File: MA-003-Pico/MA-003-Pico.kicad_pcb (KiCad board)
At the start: 2 copper layers, 49.5 x 80 mm, 5 parts, among them M1 rs485_ttl_module, M2 rs485_ttl_module, M3 rs485_ttl_module, M4 rs485_ttl_module

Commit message: Some more work
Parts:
- removed M1, M2, M3, M4: rs485_ttl_module, RS485ToTTL:rs485_ttl_module
- added H1: MountingHole_Pad, MountingHole:MountingHole_2.7mm_M2.5_DIN965_Pad, F.Cu at (138.4, 61.6)
- added H2: MountingHole_Pad, MountingHole:MountingHole_2.7mm_M2.5_DIN965_Pad, F.Cu at (175.9, 61.6)
- added H3: MountingHole_Pad, MountingHole:MountingHole_2.7mm_M2.5_DIN965_Pad, F.Cu at (177.2, 123.2)
- added H4: MountingHole_Pad, MountingHole:MountingHole_2.7mm_M2.5_DIN965_Pad, F.Cu at (139.1, 123.8)
- added J1: Power, Connector_Molex:Molex_KK-254_AE-6410-03A_1x03_P2.54mm_Vertical, F.Cu at (139.7, 68.6)
- added J2: I2C, Connector_Molex:Molex_KK-254_AE-6410-04A_1x04_P2.54mm_Vertical, F.Cu at (174.6, 76.2)
- added J3: Interface_A, Connector_IDC:IDC-Header_2x05_P2.54mm_Vertical, F.Cu at (138.4, 88.3)
- added J4: Interface_B, Connector_IDC:IDC-Header_2x05_P2.54mm_Vertical, F.Cu at (176.5, 99.1)
- added J5: Power_IB, Connector_PinHeader_2.54mm:PinHeader_1x03_P2.54mm_Vertical, F.Cu at (178.4, 107.3)
- added J6: Power_IA, Connector_PinHeader_2.54mm:PinHeader_1x03_P2.54mm_Vertical, F.Cu at (136.5, 80.0)
- added J7: Pico_On/Off, Connector_PinHeader_2.54mm:PinHeader_1x02_P2.54mm_Vertical, F.Cu at (174.6, 112.4)
- added J8: WS2812, Connector_Molex:Molex_KK-254_AE-6410-03A_1x03_P2.54mm_Vertical, F.Cu at (137.8, 109.9)
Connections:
- A1 pad 1: unconnected-(A1-GPIO0-Pad1) -> /GPIO_1
- A1 pad 10: unconnected-(A1-GPIO7-Pad10) -> /GPIO_8
- A1 pad 11: unconnected-(A1-GPIO8-Pad11) -> /GPIO_9
- A1 pad 12: unconnected-(A1-GPIO9-Pad12) -> /GPIO_10
- A1 pad 13: Net-(A1-GND-Pad13) -> /GND
- A1 pad 14: unconnected-(A1-GPIO10-Pad14) -> /GPIO_11
- A1 pad 15: unconnected-(A1-GPIO11-Pad15) -> /GPIO_12
- A1 pad 16: unconnected-(A1-GPIO12-Pad16) -> /GPIO_13
- A1 pad 17: unconnected-(A1-GPIO13-Pad17) -> /GPIO_14
- A1 pad 18: Net-(A1-GND-Pad13) -> /GND
- A1 pad 19: unconnected-(A1-GPIO14-Pad19) -> /GPIO_15
- A1 pad 2: unconnected-(A1-GPIO1-Pad2) -> /GPIO_2
- A1 pad 20: unconnected-(A1-GPIO15-Pad20) -> /GPIO_16
- A1 pad 23: Net-(A1-GND-Pad13) -> /GND
- A1 pad 28: Net-(A1-GND-Pad13) -> /GND
- A1 pad 3: Net-(A1-GND-Pad13) -> /GND
- A1 pad 30: unconnected-(A1-RUN-Pad30) -> Net-(A1-RUN)
- A1 pad 31: unconnected-(A1-GPIO26_ADC0-Pad31) -> /I2C_SDA
- A1 pad 32: unconnected-(A1-GPIO27_ADC1-Pad32) -> /I2C_SCL
- A1 pad 33: unconnected-(A1-AGND-Pad33) -> /GND
- A1 pad 34: unconnected-(A1-GPIO28_ADC2-Pad34) -> Net-(A1-GPIO28_ADC2)
- A1 pad 38: Net-(A1-GND-Pad13) -> /GND
- A1 pad 39: unconnected-(A1-VSYS-Pad39) -> /5V
- A1 pad 4: unconnected-(A1-GPIO2-Pad4) -> /GPIO_3
- A1 pad 5: unconnected-(A1-GPIO3-Pad5) -> /GPIO_4
- A1 pad 6: unconnected-(A1-GPIO4-Pad6) -> /GPIO_5
- A1 pad 7: unconnected-(A1-GPIO5-Pad7) -> /GPIO_6
- A1 pad 8: Net-(A1-GND-Pad13) -> /GND
- A1 pad 9: unconnected-(A1-GPIO6-Pad9) -> /GPIO_7
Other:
- board size 49.5 x 80 mm -> 49.5 x 68.9 mm

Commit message: Finishing the dmx ethernet pico
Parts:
- J1: value Power -> Power IN
- J3: value Interface_A -> Interface A
- moved J8 39.5 mm to (176.5, 117.5), turned to 90 degrees
- moved J7 38.4 mm to (136.5, 117.5)
- moved J6 31.8 mm to (136.5, 111.8)
- moved J5 22.2 mm to (178.4, 85.1)
- moved J3 5.08 mm to (138.4, 93.3)
- moved J4 4.44 mm to (176.5, 103.5)
- moved J2 1.88 mm to (176.5, 76.2)
- moved H2 1.42 mm to (177.2, 62.2)
- moved J1 1.40 mm to (138.4, 69.2)
- moved H4 1.27 mm to (137.8, 123.8)
- moved H1 0.90 mm to (137.8, 62.2)
- moved H3 0.64 mm to (177.2, 123.8)
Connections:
- J4 pad 2: /GPIO_9 -> /GPIO_16
- J4 pad 3: /GPIO_10 -> /GPIO_15
- J4 pad 4: /GPIO_11 -> /GPIO_14
- J4 pad 5: /GPIO_12 -> /GPIO_13
- J4 pad 6: /GPIO_13 -> /GPIO_12
- J4 pad 7: /GPIO_14 -> /GPIO_11
- J4 pad 8: /GPIO_15 -> /GPIO_10
- J4 pad 9: /GPIO_16 -> /GPIO_9
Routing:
- net /5V: track 0.00 -> 127.9 mm, vias 0 -> 5
- net /3V3: track 0.00 -> 121.9 mm
- net Net-(A1-GPIO28_ADC2): track 0.00 -> 66.1 mm, vias 0 -> 1
- net Net-(A1-RUN): track 0.00 -> 49.5 mm, vias 0 -> 1
- net /GPIO_1: track 0.00 -> 43.7 mm, vias 0 -> 1
- net /GPIO_2: track 0.00 -> 42.0 mm
- net /GPIO_15: track 0.00 -> 32.1 mm, vias 0 -> 1
- net /GPIO_9: track 0.00 -> 32.0 mm, vias 0 -> 1
- net /GND: track 0.00 -> 31.1 mm, vias 0 -> 34
- net /GPIO_4: track 0.00 -> 30.2 mm
- net /GPIO_13: track 0.00 -> 30.0 mm, vias 0 -> 1
- net /GPIO_11: track 0.00 -> 29.9 mm, vias 0 -> 1
- net /GPIO_16: track 0.00 -> 29.5 mm, vias 0 -> 1
- net /GPIO_3: track 0.00 -> 29.1 mm
- net /GPIO_6: track 0.00 -> 28.7 mm
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- added copper zone on B.Cu, net /GND
- added copper zone on F.Cu, net /GND
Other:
- board size 49.5 x 68.9 mm -> 45.7 x 68.9 mm
- board text added: "I2C"
- board text added: "Interface A"
- board text added: "Interface B"
- board text added: "On/Off"
- board text added: "Power A"
- board text added: "Power B"
- board text added: "W55RP20-EVB-PICO"
- board text added: "WS2812"

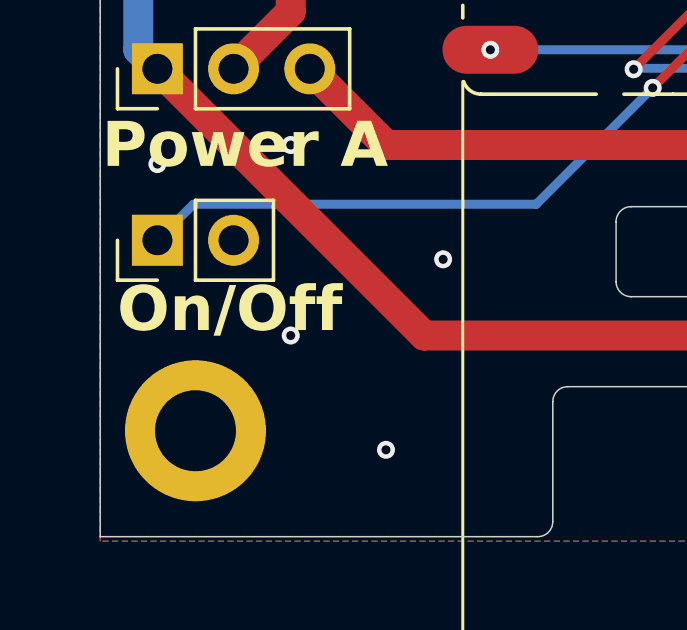
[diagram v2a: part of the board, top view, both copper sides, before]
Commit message: Generated panels, added some new PCBs
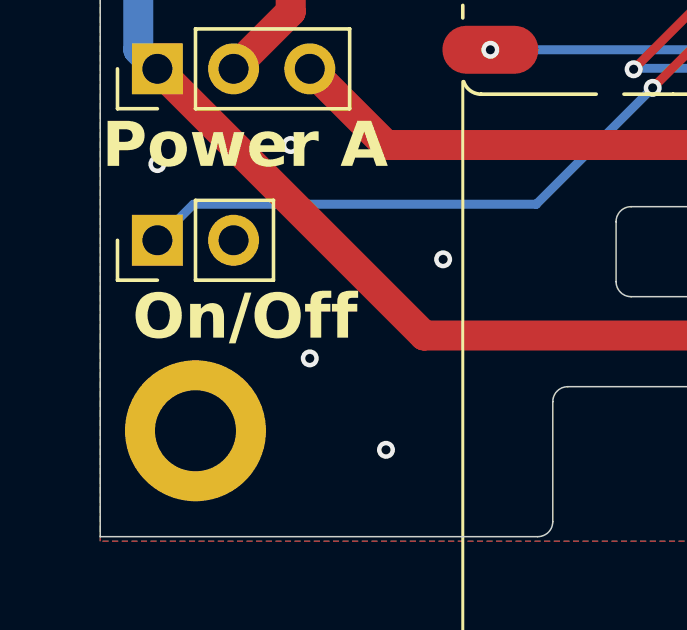
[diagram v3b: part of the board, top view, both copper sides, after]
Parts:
- J3: value Interface A -> Interface_A
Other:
- board text added: "-6.35 pin socket width from pcb"
- board text added: "MA-003/1 10.25 Jomer.dev"
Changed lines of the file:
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@@
 			)
 		)
-		(property "Value" "Interface A"
+		(property "Value" "Interface_A"
 			(at 1.27 -5.964 0)
 			(layer "F.SilkS")
@@
 	)
 	(gr_text "On/Off"
-		(at 138.938 120.65 0)
+		(at 139.446 120.904 0)
 		(layer "F.SilkS")
 		(effects
@@
 		)
 	)
+	(gr_text "MA-003/1\n10.25 Jomer.dev"
+		(at 156.337 96.901 0)
+		(layer "B.SilkS")
+		(effects
+			(font
+				(size 1.5 1.5)
+				(thickness 0.3)
+			)
+			(justify mirror)
+		)
+	)
+	(gr_text "-6.35 pin socket width from pcb"
+		(at 132.842 95.504 0)
+		(layer "Dwgs.User")
+		(effects
+			(font
+				(size 1.5 1.5)
+				(thickness 0.3)
+				(bold yes)
+			)
+			(justify right bottom)
+		)
+	)
 	(segment
 		(start 176.53 71.12)
@@
 	)
 	(via
-		(at 140.97 120.65)
+		(at 141.605 121.412)
 		(size 0.6)
 		(drill 0.3)
